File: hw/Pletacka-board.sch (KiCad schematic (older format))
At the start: 1 part

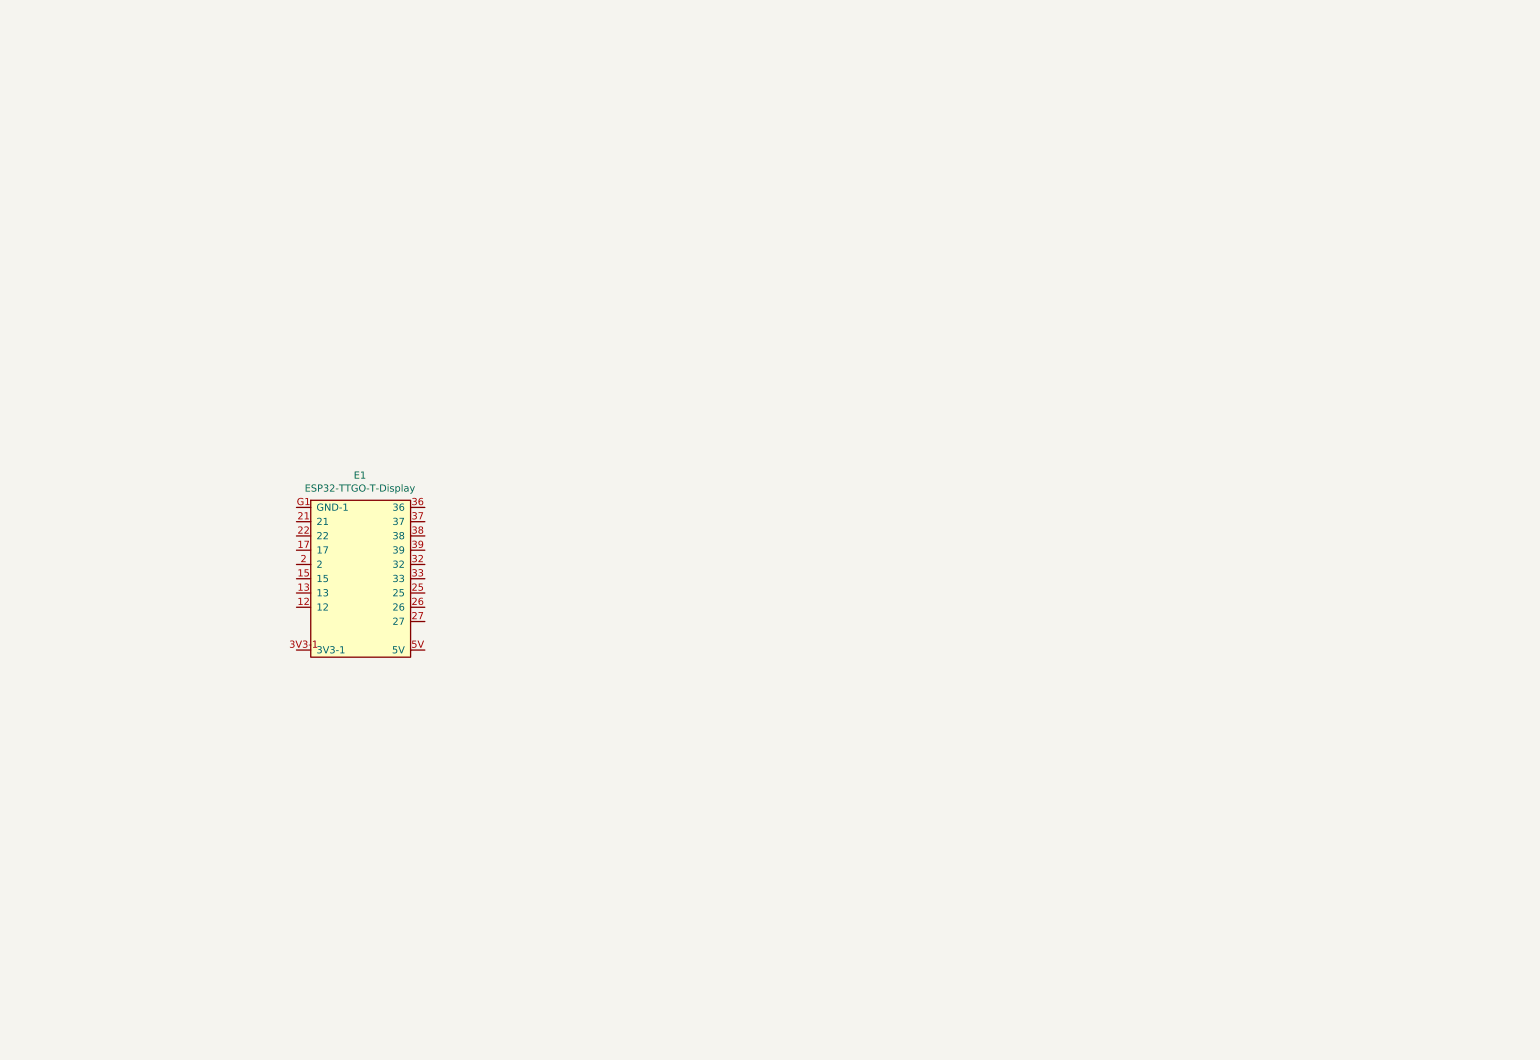
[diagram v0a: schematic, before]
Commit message: Add buttons and leds
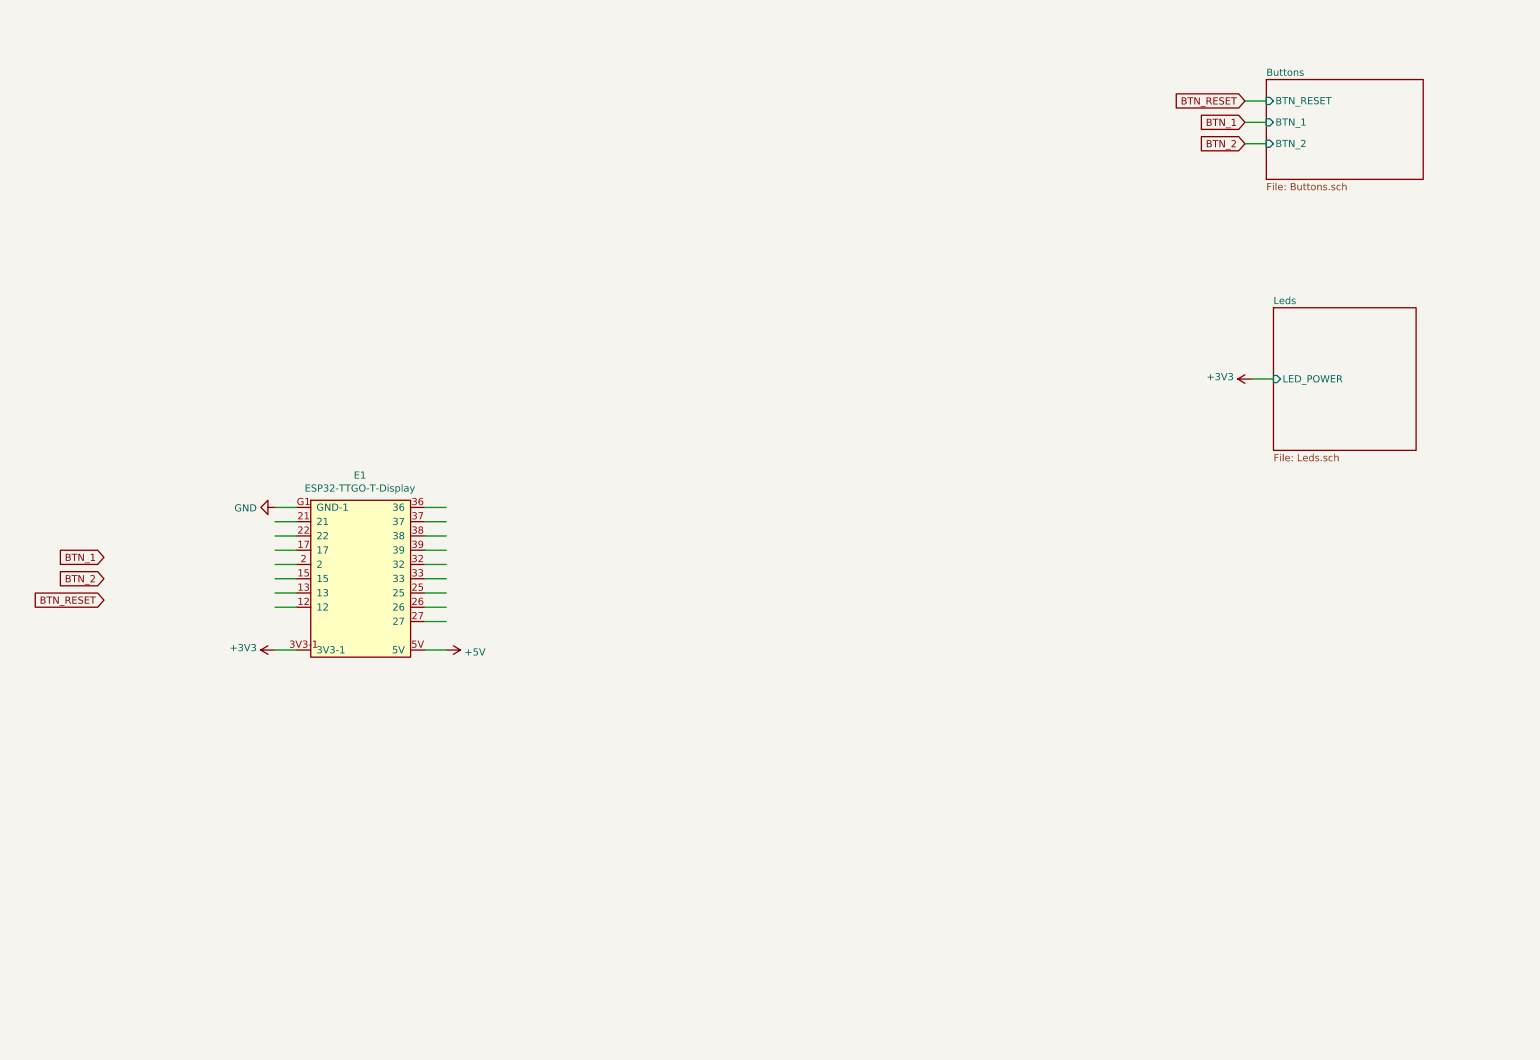
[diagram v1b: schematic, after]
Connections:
- net labels added: +3V3, +5V, BTN_1, BTN_2, BTN_RESET, GND
- wire segments 0 -> 23
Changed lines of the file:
@@
 $Descr A4 11693 8268
 encoding utf-8
-Sheet 1 1
+Sheet 1 3
 Title ""
 Date ""
@@
 	1    0    0    -1
 $EndComp
+$Comp
+L power:GND #PWR0101
+U 1 1 5F8AE428
+P 2500 3900
+F 0 "#PWR0101" H 2500 3650 50  0001 C CNN
+F 1 "GND" V 2505 3772 50  0000 R CNN
+F 2 "" H 2500 3900 50  0001 C CNN
+F 3 "" H 2500 3900 50  0001 C CNN
+	1    2500 3900
+	0    1    1    0
+$EndComp
+$Comp
+L power:+3V3 #PWR0102
+U 1 1 5F8AF0A8
+P 2500 4900
+F 0 "#PWR0102" H 2500 4750 50  0001 C CNN
+F 1 "+3V3" V 2515 5028 50  0000 L CNN
+F 2 "" H 2500 4900 50  0001 C CNN
+F 3 "" H 2500 4900 50  0001 C CNN
+	1    2500 4900
+	0    -1   -1   0
+$EndComp
+Wire Wire Line
+	2500 4900 2650 4900
+Wire Wire Line
+	2500 3900 2650 3900
+Wire Wire Line
+	3550 4900 3700 4900
+$Comp
+L power:+5V #PWR0103
+U 1 1 5F8B11B0
+P 3700 4900
+F 0 "#PWR0103" H 3700 4750 50  0001 C CNN
+F 1 "+5V" V 3715 5028 50  0000 L CNN
+F 2 "" H 3700 4900 50  0001 C CNN
+F 3 "" H 3700 4900 50  0001 C CNN
+	1    3700 4900
+	0    1    1    0
+$EndComp
+$Sheet
+S 9450 900  1100 700
+U 5F8BD394
+F0 "Buttons" 50
+F1 "Buttons.sch" 50
+F2 "BTN_RESET" I L 9450 1050 50
+F3 "BTN_1" I L 9450 1200 50
+F4 "BTN_2" I L 9450 1350 50
+$EndSheet
+Text GLabel 9300 1050 0    50   Input ~ 0
+BTN_RESET
+Wire Wire Line
+	2650 4000 2500 4000
+Wire Wire Line
+	9450 1050 9300 1050
+Text GLabel 9300 1200 0    50   Input ~ 0
+BTN_1
+Text GLabel 9300 1350 0    50   Input ~ 0
+BTN_2
+Wire Wire Line
+	9450 1200 9300 1200
+Wire Wire Line
+	9300 1350 9450 1350
+Text GLabel 1300 4250 0    50   Input ~ 0
+BTN_1
+Text GLabel 1300 4400 0    50   Input ~ 0
+BTN_2
+Text GLabel 1300 4550 0    50   Input ~ 0
+BTN_RESET
+Wire Wire Line
+	2650 4100 2500 4100
+Wire Wire Line
+	2650 4200 2500 4200
+Wire Wire Line
+	2650 4300 2500 4300
+Wire Wire Line
+	2650 4400 2500 4400
+Wire Wire Line
+	2650 4500 2500 4500
+Wire Wire Line
+	2500 4600 2650 4600
+Wire Wire Line
+	3550 3900 3700 3900
+Wire Wire Line
+	3550 4000 3700 4000
+Wire Wire Line
+	3550 4100 3700 4100
+Wire Wire Line
+	3550 4200 3700 4200
+Wire Wire Line
+	3550 4300 3700 4300
+Wire Wire Line
+	3550 4400 3700 4400
+Wire Wire Line
+	3550 4500 3700 4500
+Wire Wire Line
+	3550 4600 3700 4600
+Wire Wire Line
+	3550 4700 3700 4700
+$Sheet
+S 9500 2500 1000 1000
+U 5F8DC13F
+F0 "Leds" 50
+F1 "Leds.sch" 50
+F2 "LED_POWER" I L 9500 3000 50
+$EndSheet
+Wire Wire Line
+	9350 3000 9500 3000
+$Comp
+L power:+3V3 #PWR0104
+U 1 1 5F8DEB09
+P 9350 3000
+F 0 "#PWR0104" H 9350 2850 50  0001 C CNN
+F 1 "+3V3" V 9365 3128 50  0000 L CNN
+F 2 "" H 9350 3000 50  0001 C CNN
+F 3 "" H 9350 3000 50  0001 C CNN
+	1    9350 3000
+	0    -1   -1   0
+$EndComp
 $EndSCHEMATC

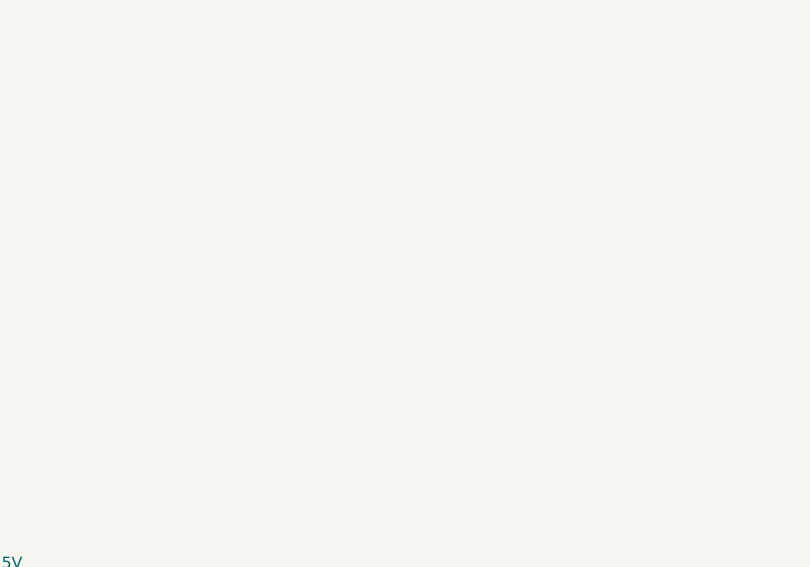
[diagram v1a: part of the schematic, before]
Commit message: Add octocoupler library
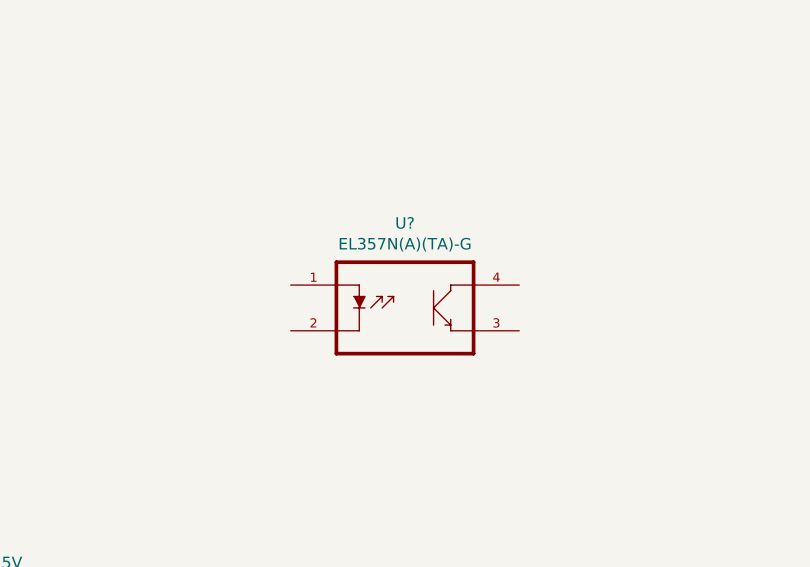
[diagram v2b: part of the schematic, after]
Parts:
- added U?: EL357N(A)(TA)-G, EL357N_A__TA_-G:SOP254P700X200-4N, symbol EL357N_A__TA_-G:EL357N(A)(TA)-G
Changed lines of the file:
@@
 	0    -1   -1   0
 $EndComp
+$Comp
+L EL357N_A__TA_-G:EL357N(A)(TA)-G U?
+U 1 1 5F8A1C73
+P 5650 3800
+F 0 "U?" H 5650 4170 50  0000 C CNN
+F 1 "EL357N(A)(TA)-G" H 5650 4079 50  0000 C CNN
+F 2 "EL357N_A__TA_-G:SOP254P700X200-4N" H 5650 3800 50  0001 L BNN
+F 3 "SOP-4 Everlight" H 5650 3800 50  0001 L BNN
+F 4 "Good" H 5650 3800 50  0001 L BNN "Field4"
+F 5 "EL357N_A__TA_-G" H 5650 3800 50  0001 L BNN "Field5"
+F 6 "Optocoupler [Everlight Electronics] EL357N_A__TA_-G Optocoupler" H 5650 3800 50  0001 L BNN "Field6"
+F 7 "IPC-7351B" H 5650 3800 50  0001 L BNN "Field7"
+F 8 "0.10 USD" H 5650 3800 50  0001 L BNN "Field8"
+F 9 "Everlight" H 5650 3800 50  0001 L BNN "Field9"
+	1    5650 3800
+	1    0    0    -1
+$EndComp
 $EndSCHEMATC

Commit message: Add libraries
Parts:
- removed U?: EL357N(A)(TA)-G, EL357N_A__TA_-G:SOP254P700X200-4N, symbol EL357N_A__TA_-G:EL357N(A)(TA)-G
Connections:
- net labels added: OPTO_FINSIHED, OPTO_STOP
- wire segments 23 -> 25
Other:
- moved on the sheet: E1
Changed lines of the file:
@@
 $Descr A4 11693 8268
 encoding utf-8
-Sheet 1 3
+Sheet 1 5
 Title ""
 Date ""
@@
 L ESP32-TTGO-T-Display:ESP32-TTGO-T-Display E1
 U 1 1 5F8A9387
-P 3000 4250
-F 0 "E1" H 3095 4825 50  0000 C CNN
-F 1 "ESP32-TTGO-T-Display" H 3095 4734 50  0000 C CNN
-F 2 "ESP32-TTGO-T-Display:ESP32-TTGO-T-Display" H 2000 4700 50  0001 C CNN
-F 3 "https://github.com/Xinyuan-LilyGO/TTGO-T-Display/blob/master/schematic/ESP32-TFT(6-26).pdf" H 2000 4700 50  0001 C CNN
-	1    3000 4250
+P 6000 3800
+F 0 "E1" H 6095 4375 50  0000 C CNN
+F 1 "ESP32-TTGO-T-Display" H 6095 4284 50  0000 C CNN
+F 2 "ESP32-TTGO-T-Display:ESP32-TTGO-T-Display" H 5000 4250 50  0001 C CNN
+F 3 "https://github.com/Xinyuan-LilyGO/TTGO-T-Display/blob/master/schematic/ESP32-TFT(6-26).pdf" H 5000 4250 50  0001 C CNN
+	1    6000 3800
 	1    0    0    -1
 $EndComp
@@
 L power:GND #PWR0101
 U 1 1 5F8AE428
-P 2500 3900
-F 0 "#PWR0101" H 2500 3650 50  0001 C CNN
-F 1 "GND" V 2505 3772 50  0000 R CNN
-F 2 "" H 2500 3900 50  0001 C CNN
-F 3 "" H 2500 3900 50  0001 C CNN
-	1    2500 3900
+P 5500 3450
+F 0 "#PWR0101" H 5500 3200 50  0001 C CNN
+F 1 "GND" V 5505 3322 50  0000 R CNN
+F 2 "" H 5500 3450 50  0001 C CNN
+F 3 "" H 5500 3450 50  0001 C CNN
+	1    5500 3450
 	0    1    1    0
 $EndComp
@@
 L power:+3V3 #PWR0102
 U 1 1 5F8AF0A8
-P 2500 4900
-F 0 "#PWR0102" H 2500 4750 50  0001 C CNN
-F 1 "+3V3" V 2515 5028 50  0000 L CNN
-F 2 "" H 2500 4900 50  0001 C CNN
-F 3 "" H 2500 4900 50  0001 C CNN
-	1    2500 4900
+P 5500 4450
+F 0 "#PWR0102" H 5500 4300 50  0001 C CNN
+F 1 "+3V3" V 5515 4578 50  0000 L CNN
+F 2 "" H 5500 4450 50  0001 C CNN
+F 3 "" H 5500 4450 50  0001 C CNN
+	1    5500 4450
 	0    -1   -1   0
 $EndComp
 Wire Wire Line
-	2500 4900 2650 4900
+	5500 4450 5650 4450
 Wire Wire Line
-	2500 3900 2650 3900
+	5500 3450 5650 3450
 Wire Wire Line
-	3550 4900 3700 4900
+	6550 4450 6700 4450
 $Comp
 L power:+5V #PWR0103
 U 1 1 5F8B11B0
-P 3700 4900
-F 0 "#PWR0103" H 3700 4750 50  0001 C CNN
-F 1 "+5V" V 3715 5028 50  0000 L CNN
-F 2 "" H 3700 4900 50  0001 C CNN
-F 3 "" H 3700 4900 50  0001 C CNN
-	1    3700 4900
+P 6700 4450
+F 0 "#PWR0103" H 6700 4300 50  0001 C CNN
+F 1 "+5V" V 6715 4578 50  0000 L CNN
+F 2 "" H 6700 4450 50  0001 C CNN
+F 3 "" H 6700 4450 50  0001 C CNN
+	1    6700 4450
 	0    1    1    0
 $EndComp
@@
 BTN_RESET
 Wire Wire Line
-	2650 4000 2500 4000
+	5650 3550 5500 3550
 Wire Wire Line
 	9450 1050 9300 1050
@@
 Wire Wire Line
 	9300 1350 9450 1350
-Text GLabel 1300 4250 0    50   Input ~ 0
+Text GLabel 4300 3800 0    50   Input ~ 0
 BTN_1
-Text GLabel 1300 4400 0    50   Input ~ 0
+Text GLabel 4300 3950 0    50   Input ~ 0
 BTN_2
-Text GLabel 1300 4550 0    50   Input ~ 0
+Text GLabel 4300 4100 0    50   Input ~ 0
 BTN_RESET
 Wire Wire Line
-	2650 4100 2500 4100
+	5650 3650 5500 3650
 Wire Wire Line
-	2650 4200 2500 4200
+	5650 3750 5500 3750
 Wire Wire Line
-	2650 4300 2500 4300
+	5650 3850 5500 3850
 Wire Wire Line
-	2650 4400 2500 4400
+	5650 3950 5500 3950
 Wire Wire Line
-	2650 4500 2500 4500
+	5650 4050 5500 4050
 Wire Wire Line
-	2500 4600 2650 4600
+	5500 4150 5650 4150
 Wire Wire Line
-	3550 3900 3700 3900
+	6550 3450 6700 3450
 Wire Wire Line
-	3550 4000 3700 4000
+	6550 3550 6700 3550
 Wire Wire Line
-	3550 4100 3700 4100
+	6550 3650 6700 3650
 Wire Wire Line
-	3550 4200 3700 4200
+	6550 3750 6700 3750
 Wire Wire Line
-	3550 4300 3700 4300
+	6550 3850 6700 3850
 Wire Wire Line
-	3550 4400 3700 4400
+	6550 3950 6700 3950
 Wire Wire Line
-	3550 4500 3700 4500
+	6550 4050 6700 4050
 Wire Wire Line
-	3550 4600 3700 4600
+	6550 4150 6700 4150
 Wire Wire Line
-	3550 4700 3700 4700
+	6550 4250 6700 4250
 $Sheet
 S 9500 2500 1000 1000
@@
 	0    -1   -1   0
 $EndComp
-$Comp
-L EL357N_A__TA_-G:EL357N(A)(TA)-G U?
-U 1 1 5F8A1C73
-P 5650 3800
-F 0 "U?" H 5650 4170 50  0000 C CNN
-F 1 "EL357N(A)(TA)-G" H 5650 4079 50  0000 C CNN
-F 2 "EL357N_A__TA_-G:SOP254P700X200-4N" H 5650 3800 50  0001 L BNN
-F 3 "SOP-4 Everlight" H 5650 3800 50  0001 L BNN
-F 4 "Good" H 5650 3800 50  0001 L BNN "Field4"
-F 5 "EL357N_A__TA_-G" H 5650 3800 50  0001 L BNN "Field5"
-F 6 "Optocoupler [Everlight Electronics] EL357N_A__TA_-G Optocoupler" H 5650 3800 50  0001 L BNN "Field6"
-F 7 "IPC-7351B" H 5650 3800 50  0001 L BNN "Field7"
-F 8 "0.10 USD" H 5650 3800 50  0001 L BNN "Field8"
-F 9 "Everlight" H 5650 3800 50  0001 L BNN "Field9"
-	1    5650 3800
-	1    0    0    -1
-$EndComp
+$Sheet
+S 9500 4000 1000 1500
+U 5F8B0B95
+F0 "Optocoupler" 50
+F1 "Optocoupler.sch" 50
+F2 "OPTO_FINSIHED" I L 9500 4400 50
+F3 "OPTO_STOP" I L 9500 4900 50
+$EndSheet
+Text GLabel 9350 4400 0    50   Input ~ 0
+OPTO_FINSIHED
+Text GLabel 9350 4900 0    50   Input ~ 0
+OPTO_STOP
+Wire Wire Line
+	9350 4400 9500 4400
+Wire Wire Line
+	9500 4900 9350 4900
+Text GLabel 4300 4300 0    50   Input ~ 0
+OPTO_FINSIHED
+Text GLabel 4300 4450 0    50   Input ~ 0
+OPTO_STOP
+$Sheet
+S 1000 1000 1000 1500
+U 5F8F7408
+F0 "Power" 50
+F1 "Power.sch" 50
+$EndSheet
 $EndSCHEMATC

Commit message: Add connectors
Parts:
- added J4: Conn_01x02_Female, Terminal_block:TerminalBlock_Phoenix_PT-1,5-2-5.0-H_1x02_P5.00mm_Horizontal, symbol Connector:Conn_01x02_Female
- added J5: Conn_01x03_Female, Terminal_block:TerminalBlock_Phoenix_PT-1,5-3-5.0-H_1x03_P5.00mm_Horizontal, symbol Connector:Conn_01x03_Female
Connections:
- net labels added: OPTO_FINISHED_IN_MINUS, OPTO_FINISHED_IN_PLUS, OPTO_STOP_IN_MINUS, OPTO_STOP_IN_PLUS, VCC
- wire segments 25 -> 32
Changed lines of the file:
@@
 F1 "Power.sch" 50
 $EndSheet
+$Comp
+L Connector:Conn_01x02_Female J4
+U 1 1 5F9151EB
+P 2550 5600
+F 0 "J4" V 2488 5412 50  0000 R CNN
+F 1 "Conn_01x02_Female" V 2397 5412 50  0000 R CNN
+F 2 "Terminal_block:TerminalBlock_Phoenix_PT-1,5-2-5.0-H_1x02_P5.00mm_Horizontal" H 2550 5600 50  0001 C CNN
+F 3 "~" H 2550 5600 50  0001 C CNN
+	1    2550 5600
+	0    -1   -1   0
+$EndComp
+$Comp
+L Connector:Conn_01x03_Female J5
+U 1 1 5F915FED
+P 3700 5600
+F 0 "J5" V 3638 5412 50  0000 R CNN
+F 1 "Conn_01x03_Female" V 3547 5412 50  0000 R CNN
+F 2 "Terminal_block:TerminalBlock_Phoenix_PT-1,5-3-5.0-H_1x03_P5.00mm_Horizontal" H 3700 5600 50  0001 C CNN
+F 3 "~" H 3700 5600 50  0001 C CNN
+	1    3700 5600
+	0    -1   -1   0
+$EndComp
+Wire Wire Line
+	2550 5950 2550 5800
+Wire Wire Line
+	2650 5950 2650 5800
+Wire Wire Line
+	3600 5950 3600 5800
+Wire Wire Line
+	3700 5950 3700 5800
+Wire Wire Line
+	3800 5950 3800 5800
+Text GLabel 2550 5950 3    50   Input ~ 0
+OPTO_STOP_IN_PLUS
+Text GLabel 2650 5950 3    50   Input ~ 0
+OPTO_STOP_IN_MINUS
+Text GLabel 3600 5950 3    50   Input ~ 0
+OPTO_FINISHED_IN_MINUS
+Text GLabel 3700 5950 3    50   Input ~ 0
+OPTO_FINISHED_IN_PLUS
+Wire Wire Line
+	3800 5950 3900 5950
+Wire Wire Line
+	3600 5950 3500 5950
+$Comp
+L power:GND #PWR0116
+U 1 1 5F91B916
+P 3500 5950
+F 0 "#PWR0116" H 3500 5700 50  0001 C CNN
+F 1 "GND" V 3505 5822 50  0000 R CNN
+F 2 "" H 3500 5950 50  0001 C CNN
+F 3 "" H 3500 5950 50  0001 C CNN
+	1    3500 5950
+	0    1    1    0
+$EndComp
+$Comp
+L power:VCC #PWR0117
+U 1 1 5F91BD5C
+P 3900 5950
+F 0 "#PWR0117" H 3900 5800 50  0001 C CNN
+F 1 "VCC" V 3917 6078 50  0000 L CNN
+F 2 "" H 3900 5950 50  0001 C CNN
+F 3 "" H 3900 5950 50  0001 C CNN
+	1    3900 5950
+	0    1    1    0
+$EndComp
 $EndSCHEMATC
